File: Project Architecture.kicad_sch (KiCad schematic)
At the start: 0 parts

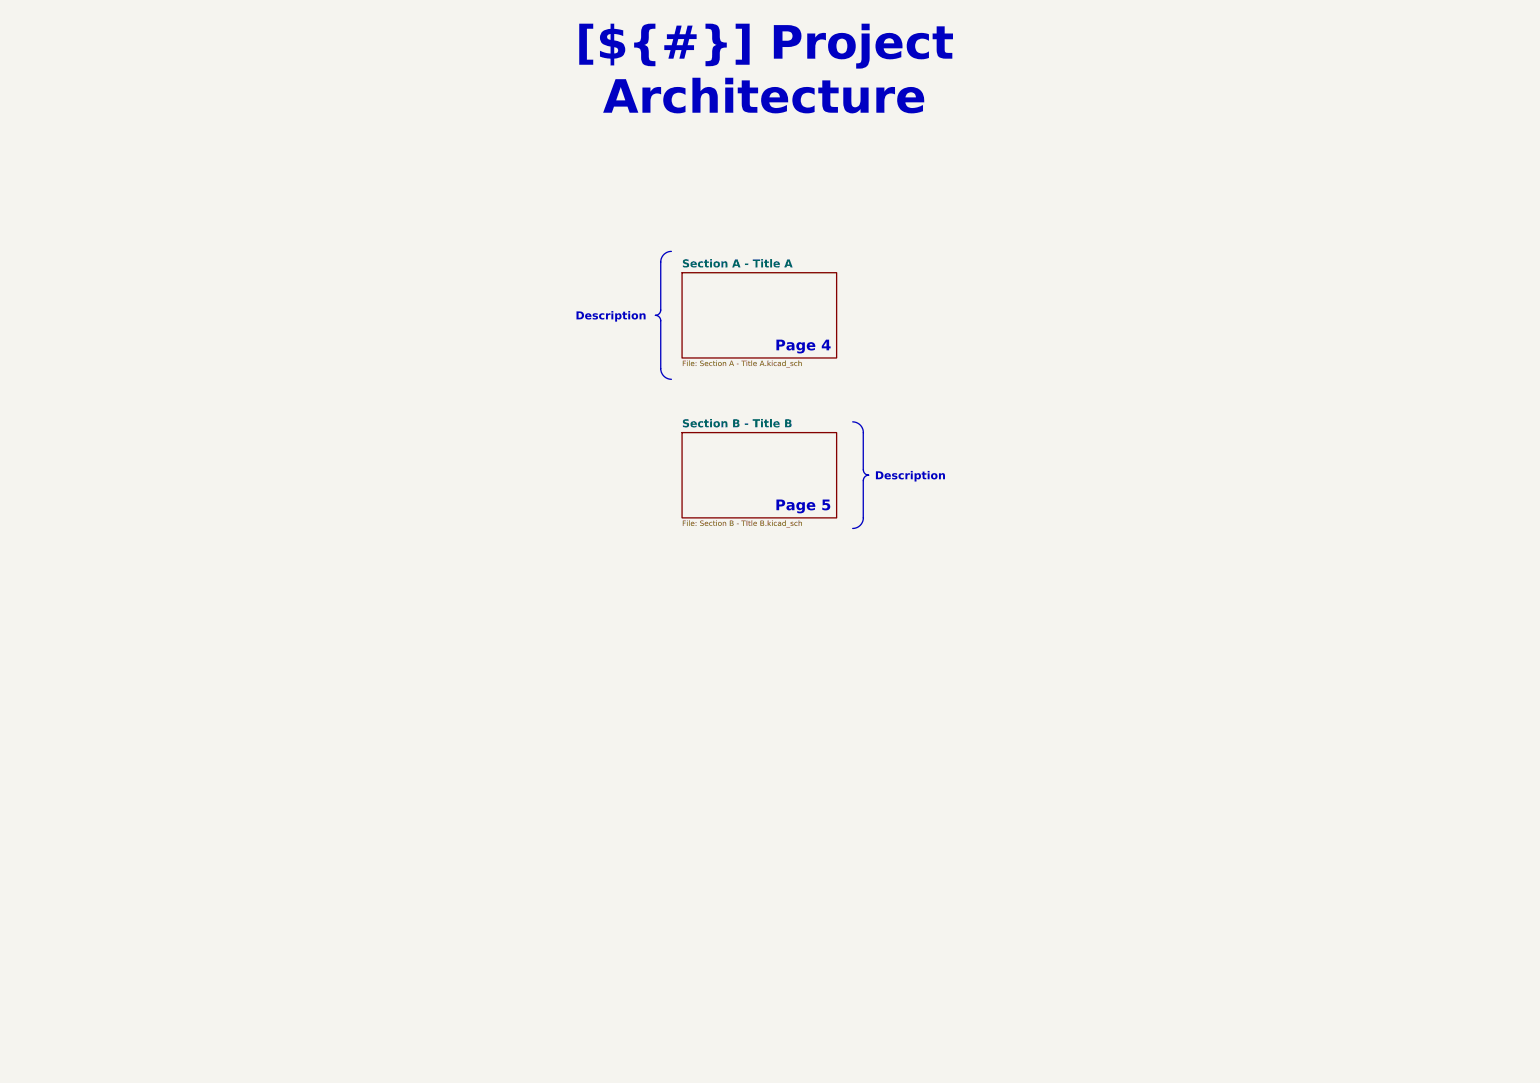
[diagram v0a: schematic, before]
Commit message: feat(sch): preliminary Tessera Badge schematic
- Add sheets for LEDs, USB connector, MCU, NFC, power and STSAFE-A120.
- Drop the old placeholder sections.
- Bump the lib submodule and add IPN as a BOM column in the kibot
  outputs to reflect the DB-library parts now placed in the schematic.
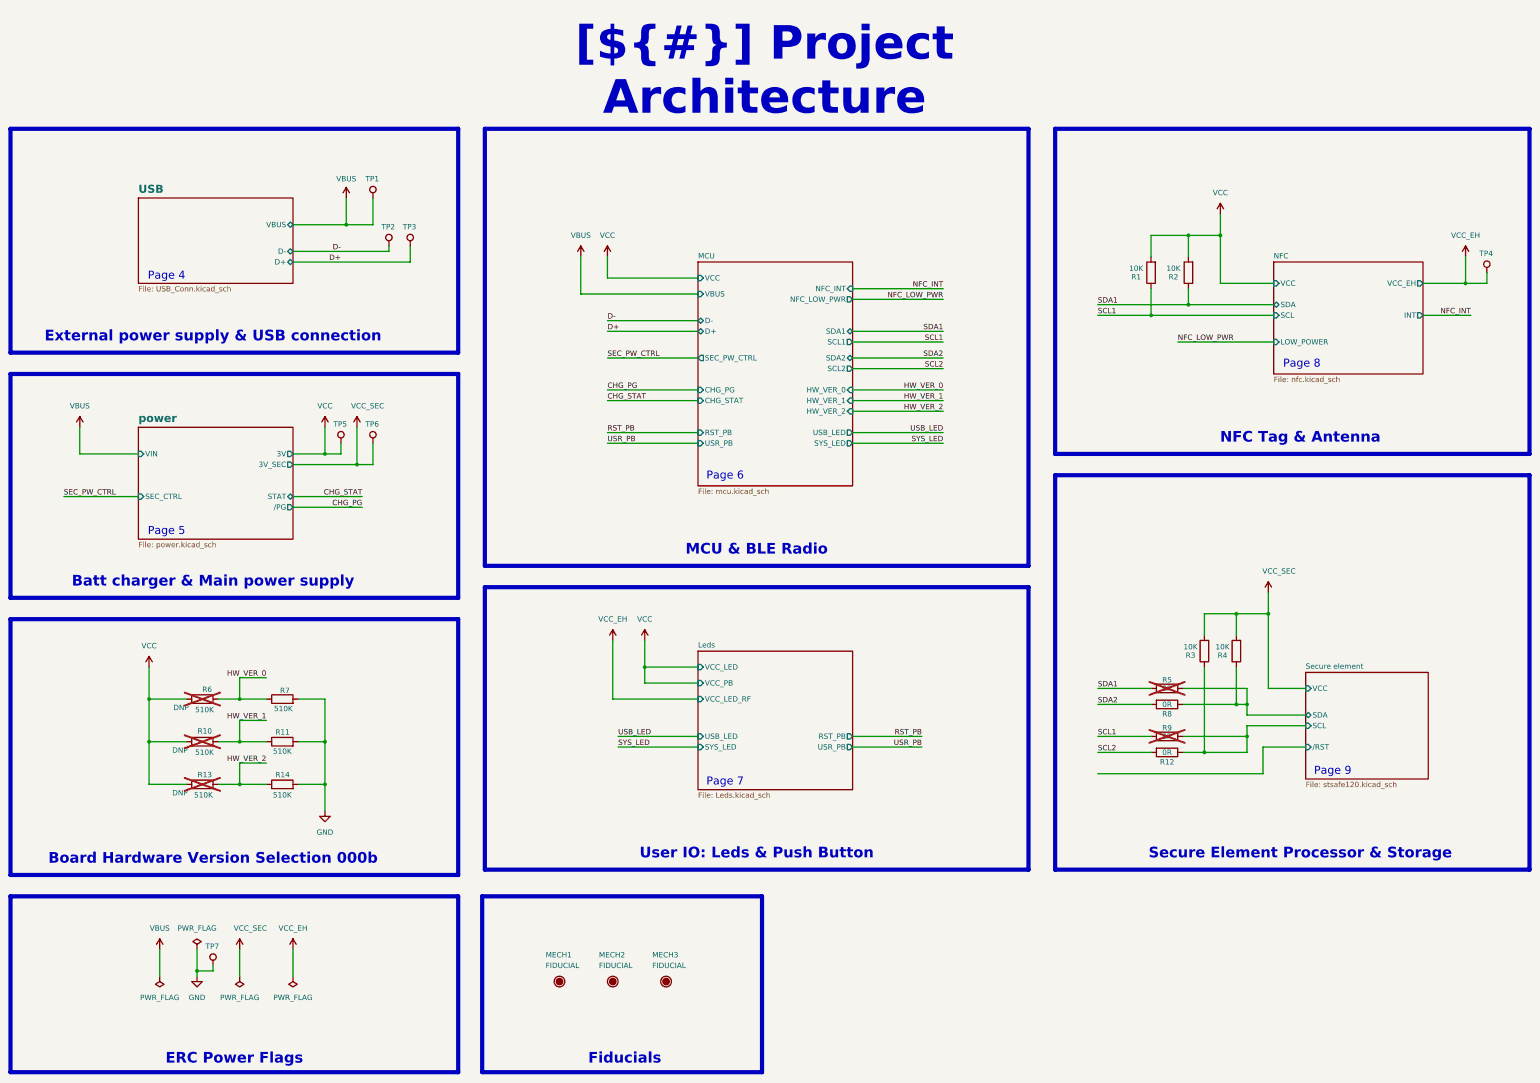
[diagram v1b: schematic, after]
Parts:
- added MECH1, MECH2, MECH3: FIDUCIAL, Mechanical:Fiducial_1mm_Mask2mm, symbol catalog:Mechanical/FIDUCIAL_D1_0mm_Mask_2_0mm
- added R1, R2, R3, R4: 10 kOhms, Resistor_SMD:R_0402_1005Metric, symbol catalog:Resistors/R0402_10K_0.063W_±1%
- added R10, R11, R13, R14, R6, R7: 510 kOhms, Resistor_SMD:R_0402_1005Metric, symbol catalog:Resistors/R0402_510K_0.063W_±1%
- added R12, R5, R8, R9: 0R ±5% 1/10W, Resistor_SMD:R_0603_1608Metric, symbol catalog:Resistors/R0603_0R_0.1W_±5%
- added TP1, TP2, TP3, TP4, TP5, TP6, TP7: TP, Test:TestPoint_Pad_D1.0mm, symbol catalog:Test Points/TP_SMD_D1_0mm
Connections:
- new net D+: TP3.1
- new net D-: TP2.1
- new net GND: R11.2, R14.2, R7.2, TP7.1
- new net HW_VER_0: R6.2, R7.1
- new net HW_VER_1: R10.2, R11.1
- new net HW_VER_2: R13.2, R14.1
- new net SCL1: R1.1, R9.2
- new net SCL2: R12.2
- new net SDA1: R2.1, R5.2
- new net SDA2: R8.2
- new net Secure element/SCL: R12.1, R3.1, R9.1
- new net Secure element/SDA: R4.1, R5.1, R8.1
- new net VBUS: TP1.1
- new net VCC: R1.2, R10.1, R13.1, R2.2, R6.1, TP5.1
- new net VCC_EH: TP4.1
- new net VCC_SEC: R3.2, R4.2, TP6.1
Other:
- sheet Section A - Title A renamed USB
- removed sheet Section B - Title B
- added sheet Leds (Leds.kicad_sch)
- added sheet MCU (mcu.kicad_sch)
- added sheet NFC (nfc.kicad_sch)
- added sheet Secure element (stsafe120.kicad_sch)
- added sheet power (power.kicad_sch)
- sheet USB: file Section A - Title A.kicad_sch -> USB_Conn.kicad_sch
- sheet USB ports: added D+, D-, VBUS; removed none
- note added: "Page 6"
- note added: "Page 7"
- note added: "Page 8"
- note added: "Page 9"

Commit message: fix(hardware): replace jumper/passive footprints with 0402 and refine schematics
- Replace 0-ohm jumper resistors with 0402 package equivalents
- Reduce package size on several capacitors
- Correct and simplify several schematic symbols (replaced with
  simplified equivalents where the original was overcomplicated)
- Bump lib submodule to the updated component library (renamed
  switch footprints, new Conn_01x02_MountingPin symbol, pad/pin
  numbering fixes, approved IPN assignments, Workart artwork library)
- Register Workart.pretty in fp-lib-table
- Mark J3 as DNP in mcu.kicad_sch
- Continue schematic wiring/placement (Leds.kicad_sch, tessera.kicad_sch)
  and PCB routing/placement (tessera.kicad_pcb)
- Add board outline source (Images/pcb_size.dxf, pcb_shape.FCStd) and
  silkscreen artwork sources (Logos/) for the Workart footprints
- Complete preliminary version of PCB
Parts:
- removed R12, R5, R8, R9: 0R ±5% 1/10W, Resistor_SMD:R_0603_1608Metric, symbol catalog:Resistors/R0603_0R_0.1W_±5%
- added R12, R5, R8, R9: 0R ±5% 1/16W, Resistor_SMD:R_0402_1005Metric, symbol catalog:Resistors/R0402_0R_0.1W_±5%
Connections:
- net SCL1: now also R9.1
- net SCL2: now also R12.2
- net SDA1: now also R5.1
- net SDA2: now also R8.2
- net Secure element/SCL: now also R12.1, R9.2
- net Secure element/SDA: now also R5.2, R8.1
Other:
- sheet MCU ports: added SEC_RST; removed none

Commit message: fix(hardware): resolve KiBot iBoM crash and stale symbol warning
- Add G1-G5 Workart artwork as schematic symbols marked exclude-from-BOM,
  instead of PCB-only footprints.
- Works around a KiBot iBoM crash caused by PCB-only footprints having
  no parent sheet in the variant netlist  (upstream: INTI-CMNB/KiBot#955)
- Register the Workart.kicad_sym library in sym-lib-table
- Bump lib submodule to add the matching Workart schematic symbols
- Fix W043 warning: remove stale lib_name override for J2 in
  power.kicad_sch
- CI: checkout submodules recursively and regenerate catalog.sqlite
  from lib_db/source/*.csv (lib/lib_db/build_db.py) so the "catalog"
  database library resolves during CI runs
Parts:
- added G1: WA_APS_Logo, Workart:logo_aps_4_5, symbol Workart:WA_APS_Logo
- added G2: WA_tessera_Name, Workart:Name, symbol Workart:WA_tessera_Name
- added G3: WA_tessera_light_bulb, Workart:light_bulb_8_7_12, symbol Workart:WA_tessera_light_bulb
- added G4: WA_tessera_linkedin_qr, Workart:linkedin_qr_with_linkedin_logo_inv, symbol Workart:WA_tessera_linkedin_qr
- added G5: WA_tessera_binary, Workart:bin_logo, symbol Workart:WA_tessera_binary

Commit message: feat(hardware): add fiducial markers on bottom layer, add via stich and teardrops
- Add FIDUCIAL_D1_0mm_Mask_2_0mm reference marks to Project
  Architecture.kicad_sch and place the corresponding
  Fiducial_1mm_Mask2mm footprints on the PCB (for pick & place
  alignment)
- Added via stiching network
- Added teardrops
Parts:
- added MECH4, MECH5, MECH6: FIDUCIAL, Mechanical:Fiducial_1mm_Mask2mm, symbol catalog:Mechanical/FIDUCIAL_D1_0mm_Mask_2_0mm
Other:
- moved on the sheet: MECH1, MECH2, MECH3
